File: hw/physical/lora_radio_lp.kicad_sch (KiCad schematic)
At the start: 0 parts

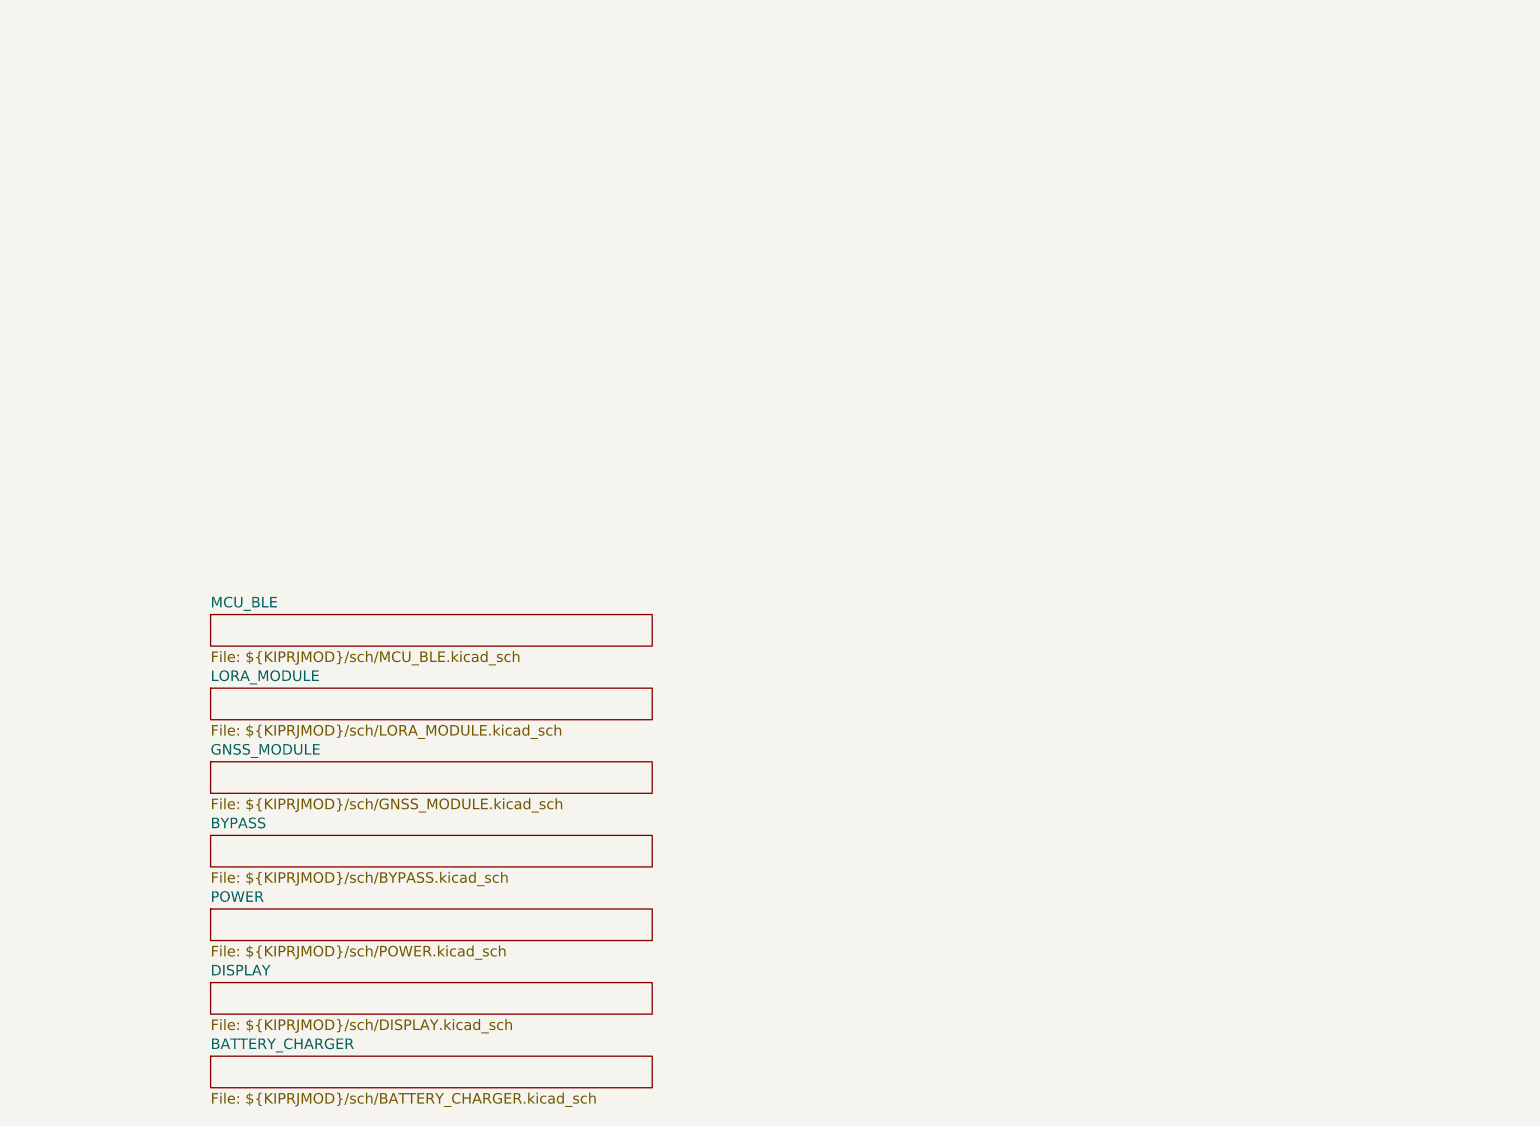
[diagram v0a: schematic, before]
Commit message: Removed sch subdirectory.
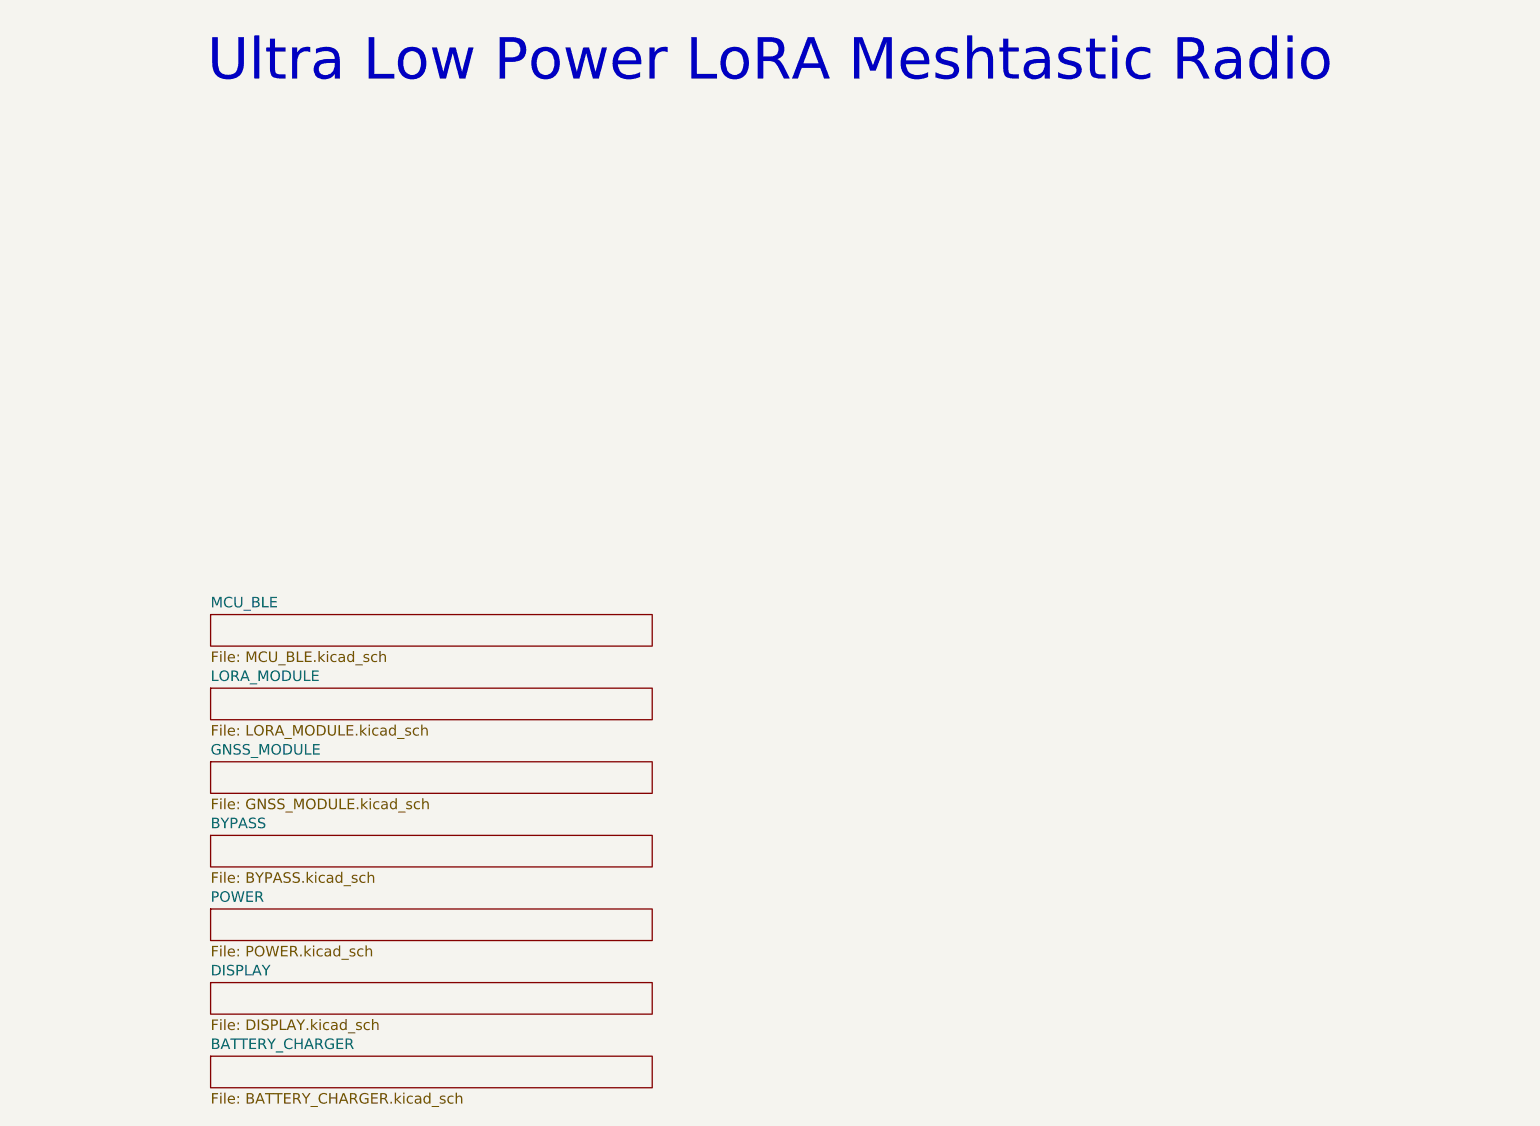
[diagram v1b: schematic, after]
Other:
- sheet BATTERY_CHARGER: file ${KIPRJMOD}/sch/BATTERY_CHARGER.kicad_sch -> BATTERY_CHARGER.kicad_sch
- sheet BYPASS: file ${KIPRJMOD}/sch/BYPASS.kicad_sch -> BYPASS.kicad_sch
- sheet DISPLAY: file ${KIPRJMOD}/sch/DISPLAY.kicad_sch -> DISPLAY.kicad_sch
- sheet GNSS_MODULE: file ${KIPRJMOD}/sch/GNSS_MODULE.kicad_sch -> GNSS_MODULE.kicad_sch
- sheet LORA_MODULE: file ${KIPRJMOD}/sch/LORA_MODULE.kicad_sch -> LORA_MODULE.kicad_sch
- sheet MCU_BLE: file ${KIPRJMOD}/sch/MCU_BLE.kicad_sch -> MCU_BLE.kicad_sch
- sheet POWER: file ${KIPRJMOD}/sch/POWER.kicad_sch -> POWER.kicad_sch
- note added: "Ultra Low Power LoRA Meshtastic Radio"
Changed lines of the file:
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@@
 		(rev "Proto")
+	)
+	(text "Ultra Low Power LoRA Meshtastic Radio"
+		(exclude_from_sim no)
+		(at 103.124 29.718 0)
+		(effects
+			(font
+				(size 5 5)
+			)
+		)
 	)
 	(sheet
@@
 			)
 		)
-		(property "Sheetfile" "${KIPRJMOD}/sch/MCU_BLE.kicad_sch"
+		(property "Sheetfile" "MCU_BLE.kicad_sch"
 			(at 35.56 100.9146 0)
 			(effects
@@
 			)
 		)
-		(property "Sheetfile" "${KIPRJMOD}/sch/BYPASS.kicad_sch"
+		(property "Sheetfile" "BYPASS.kicad_sch"
 			(at 35.56 127.5846 0)
 			(effects
@@
 			)
 		)
-		(property "Sheetfile" "${KIPRJMOD}/sch/POWER.kicad_sch"
+		(property "Sheetfile" "POWER.kicad_sch"
 			(at 35.56 136.4746 0)
 			(effects
@@
 			)
 		)
-		(property "Sheetfile" "${KIPRJMOD}/sch/GNSS_MODULE.kicad_sch"
+		(property "Sheetfile" "GNSS_MODULE.kicad_sch"
 			(at 35.56 118.6946 0)
 			(effects
@@
 			)
 		)
-		(property "Sheetfile" "${KIPRJMOD}/sch/LORA_MODULE.kicad_sch"
+		(property "Sheetfile" "LORA_MODULE.kicad_sch"
 			(at 35.56 109.8046 0)
 			(effects
@@
 			)
 		)
-		(property "Sheetfile" "${KIPRJMOD}/sch/BATTERY_CHARGER.kicad_sch"
+		(property "Sheetfile" "BATTERY_CHARGER.kicad_sch"
 			(at 35.56 154.2546 0)
 			(effects
@@
 			)
 		)
-		(property "Sheetfile" "${KIPRJMOD}/sch/DISPLAY.kicad_sch"
+		(property "Sheetfile" "DISPLAY.kicad_sch"
 			(at 35.56 145.3646 0)
 			(effects
